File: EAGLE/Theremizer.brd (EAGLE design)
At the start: 160 x 100 mm, 121 parts, among them IC2 NE5532D, IC3 TL072D, J1 3x2 M, J2 1x6 M, J3 AUDIO_JACK_TRS_0.25"_PTH_RA, J4 POWER_JACK, J5 AUDIO_JACK_TRS_0.25"_PTH_RA, Q1 PMV45EN2R, Q2 J310, Q3 J310, Q4 J310, Q6 2N5088, Q7 2N5088, SW1 !RESET, U1 NCP1117ST50T3G, U2 MCU-ATMEGA328P-AU(TQFP32), U4 LTC2645CMS-L8PBF, X1 16 MHz

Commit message: Inital board & bunch of schematic changes
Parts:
- moved H1 255.4 mm to (156.2, 24.1)
- moved H2 253.3 mm to (156.2, 74.9)
- moved C6 198.0 mm to (87.6, 57.1), turned to 180 degrees
- moved TP6 197.4 mm to (88.9, 72.4)
- moved C28 190.1 mm to (119.4, 92.7)
- moved C20 186.0 mm to (57.1, 5.08), turned to 270 degrees
- moved R42 185.6 mm to (115.6, 83.8)
- moved TP5 185.1 mm to (81.3, 72.4)
- moved C15 184.7 mm to (124.5, 96.5)
- moved TP4 183.9 mm to (85.1, 72.4)
- moved C5 175.5 mm to (71.1, 63.5)
- moved J2 175.3 mm to (86.4, 80.0), turned to 180 degrees
- moved R38 173.0 mm to (124.5, 92.7)
- moved C4 169.6 mm to (71.1, 67.3)
- moved TP3 166.8 mm to (72.4, 72.4)
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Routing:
- net GND: track 0.00 -> 818.7 mm, vias 0 -> 2
- net +15V: track 0.00 -> 365.8 mm, vias 0 -> 1
- net -15V: track 0.00 -> 279.4 mm, vias 0 -> 2
- net +5V: track 0.00 -> 212.9 mm, vias 0 -> 3
- net N$52: track 0.00 -> 125.0 mm, vias 0 -> 1
- net N$19: track 0.00 -> 106.4 mm, vias 0 -> 2
- net RES_CV: track 0.00 -> 100.7 mm, vias 0 -> 6
- net N$50: track 0.00 -> 90.5 mm, vias 0 -> 2
- net N$24: track 0.00 -> 89.2 mm
- net N$6: track 0.00 -> 85.3 mm
- net THEREMIN_OUT: track 0.00 -> 79.6 mm, vias 0 -> 2
- net N$28: track 0.00 -> 78.5 mm
- net N$11: track 0.00 -> 75.8 mm, vias 0 -> 1
- net FREQ_CV: track 0.00 -> 74.8 mm, vias 0 -> 2
- net N$12: track 0.00 -> 71.6 mm, vias 0 -> 2
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- added copper zone on layer 1, net GND
- added copper zone on layer 16, net GND

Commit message: Package size change
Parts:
- C10, C12, C9: device rcl:C0402 -> rcl:C0805
- C18: value 100nF -> 100n
- C25: value (none) -> 100n
- IC1: value (none) -> AS3320
- R10, R12, R13, R14, R15, R16, R17, R18, R19, R21, R22, R23, R46, R48, R7, R9: device rcl:R0402 -> rcl:R0805
- U3: value (none) -> DCWN03B-15
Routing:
- net -15V: track 279.4 -> 280.9 mm
- net FILTER_OUTPUT: track 51.5 -> 52.8 mm
- net N$13: track 17.0 -> 18.3 mm
- net N$10: track 62.5 -> 63.4 mm
- net N$14: track 30.2 -> 31.1 mm
- net N$7: track 45.6 -> 46.5 mm

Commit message: Almost complete BOM
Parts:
- C11, C13, C14, C15, C16, C17, C18, C19, C20, C21, C23, C24, C25, C26, C27, C28, C29, C30, C31, C32: device rcl:C0402 -> rcl:C0805
- R24, R25, R28, R29, R30, R31, R32, R33, R38, R39, R40, R41, R42: device rcl:R0402 -> rcl:R0805
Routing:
- net GND: track 819.0 -> 821.6 mm
- net +15V: track 365.8 -> 368.0 mm
- net N$31: track 12.2 -> 13.5 mm
- net N$44: track 44.7 -> 45.6 mm
- net N$49: track 24.4 -> 25.3 mm
- net N$28: track 78.5 -> 79.4 mm
- net N$29: track 39.6 -> 40.5 mm
- net N$42: track 2.66 -> 1.91 mm
- net N$45: track 21.5 -> 22.1 mm
- net N$43: track 5.86 -> 6.38 mm
- net N$25: track 3.32 -> 3.84 mm

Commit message: Test point for filter out
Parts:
- added FILTER_OUT: TPB2,54, testpad:B2,54
- C1, C2, C3, C35, C4, C5, C6, C7, C8: device rcl:C0805K -> rcl:C0805
- C10, C12, C13, C21, C9: value 300pF -> 300p
- C20: value 100nF -> 100n
- C33, C34: value (none) -> 8-100p
- L2: value 10mH -> 10m
- R11: device rcl:R0402 -> rcl:R0805
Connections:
- net FILTER_OUTPUT: now also FILTER_OUT.TP

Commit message: Added bypass, new mixer
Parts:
- removed MX1: ADE-1, minickts (1):CD636
- added $U1: SA602AD, SA602AN:SO8
- added C36, C37: 0.1u, rcl:C0805
- added C38, C39: 10u, rcl:C0805
- added C40, C41: 10n, rcl:C0805
- added D4: M7, diode:SMB
- added IC4: NE5532D, linear:SO08
- added LD1: (no value), led:DUOLED-C-5MM
- added R20, R49: 0, rcl:R0805
- added R50: 10k, rcl:R0805
- added S2: SWITCH-3PDT-PTH-STOMP, SparkFun-Switches:STOMP_SWITCH_3PDT
- C18, C20, C25: value 100n -> 0.1u
- C21: value 300p -> 470n
- C23: value 2.2nF -> 2.2n
- C24: value 470pF -> 470p
- C26: value 10uF -> 10u
- C27: value 10n -> 200p
- C28: value 10n -> 4.7n
- C31: value 100u -> 1000u
- C34: value 8-100p -> 50-100p
- R25, R30: value 100 -> 100k
- R26: value 10k -> 1k; device pot:PT-10 -> rcl:R0805
- R34: value 10k -> 22k
- R35: device pot:PT-10 -> rcl:R0805
- R38, R39: value 470 -> 470k
- R41, R42: value 10k -> 100k
- R8: value DNP or 0 -> 0
- moved R26 329.9 mm to (-156.2, -61.0), turned to 0 degrees
- moved R35 315.2 mm to (-165.1, -92.7), turned to 0 degrees
- moved C27 278.4 mm to (-156.2, -54.6), turned to 0 degrees
- moved FILTER_OUT 179.5 mm to (6.35, 21.6)
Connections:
- removed net 9V: J4.PWR, U3.22, U3.23
- removed net AUDIO_INPUT: C11.1, J5.RING-NORM
- removed net N$32 (its old number): C15.1, C34.1
- new net +9V: $U1.8, S2.P$8
- new net AUDIO_IN: C11.1, S2.P$3
- new net N$38: R50.1, S2.P$4
- new net N$51: D1.A, D4.A, J4.PWR
- new net N$54: D4.C, U3.22, U3.23
- new net N$55: R20.1, U3.14
- new net N$56: R49.1, U3.11
- new net N$57: C26.1, L3.1, R29.2
- new net N$58: LD1.AX, S2.P$9
- new net OUTPUT: IC3.7, J3.RING-NORM, J3.TIP-NORM, R47.A, R47.S, S2.P$1, S2.P$6
- net +15V: now also C36.1, C37.1, C38.1, C39.1, IC4.8, R20.2; no longer D1.A, U3.14
- net -15V: now also R49.2; no longer IC2.4, U3.11
- net FILTER_OUTPUT: now also S2.P$5
- net GND: now also $U1.3, $U1.5, $U1.6, $U1.7, C15.1, C26.2, C36.2, C37.2, C38.2, C39.2, C40.1, IC2.4, IC4.4, LD1.C, Q2.G, Q3.G, R34.S, R50.2; no longer C27.2, J3.TIP-NORM, J5.SLEEVE-NORM, J5.TIP-NORM, MX1.1, MX1.4, MX1.5
- net N$22: now also C15.2
- net N$24: now also $U1.1; no longer MX1.6
- net N$26: now also C24.1, C27.1, L3.2, Q3.D; no longer C26.1, L3.1, R29.2
- net N$27: now also C27.2; no longer C24.1, L3.2, Q3.D
- net N$29: now also IC4.3; no longer IC2.5
- net N$33: now also C32.1, R35.2; no longer C15.2, Q2.G
- net N$35: now also C34.1
- net N$36: now also $U1.2; no longer MX1.3
- net N$37: now also J5.RING-NORM, J5.TIP-NORM, S2.P$2; no longer C26.2, Q3.G
- net N$39: now also R26.2; no longer R26.E
- net N$40: now also R26.1; no longer R26.A
- net N$47: now also J5.SLEEVE-NORM; no longer C32.1, R35.E
- net N$48: now also IC4.2, R35.1; no longer IC2.6, R35.A
- net N$49: now also IC4.1; no longer IC2.7
- net N$53: now also LD1.AR, S2.P$7; no longer IC3.7, J3.RING-NORM, R47.A, R47.S
- net THEREMIN_OUT: now also $U1.4, C40.2, C41.1, C41.2; no longer C27.1, MX1.2
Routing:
- net OUTPUT: track 0.00 -> 50.5 mm
- net N$53: track 50.5 -> 0.00 mm
- net N$57: track 0.00 -> 36.6 mm, vias 0 -> 2
- net GND: track 821.7 -> 788.5 mm
- net N$26: track 53.5 -> 20.8 mm, vias 2 -> 0
- net N$32 (its old number): track 24.4 -> 0.00 mm
- net N$24: track 88.9 -> 64.9 mm
- net N$40: track 30.3 -> 6.83 mm
- net N$27: track 21.1 -> 0.00 mm
- net N$36: track 20.8 -> 0.00 mm
- net 9V: track 20.5 -> 0.00 mm
- net AUDIO_INPUT: track 14.8 -> 0.00 mm
- net N$37: track 4.21 -> 17.3 mm
- net +15V: track 368.0 -> 356.9 mm
- net N$47: track 24.8 -> 14.2 mm
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
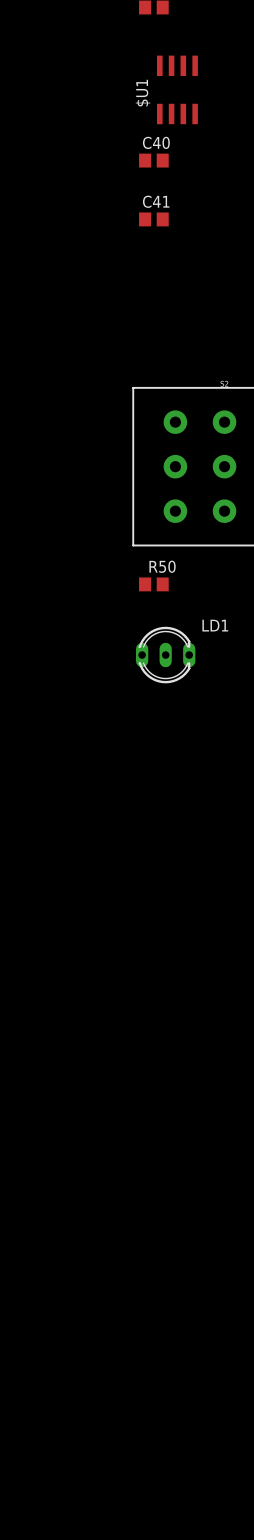
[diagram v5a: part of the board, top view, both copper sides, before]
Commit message: Changed cap values for mixer output, added decoupling caps, 9V regulator
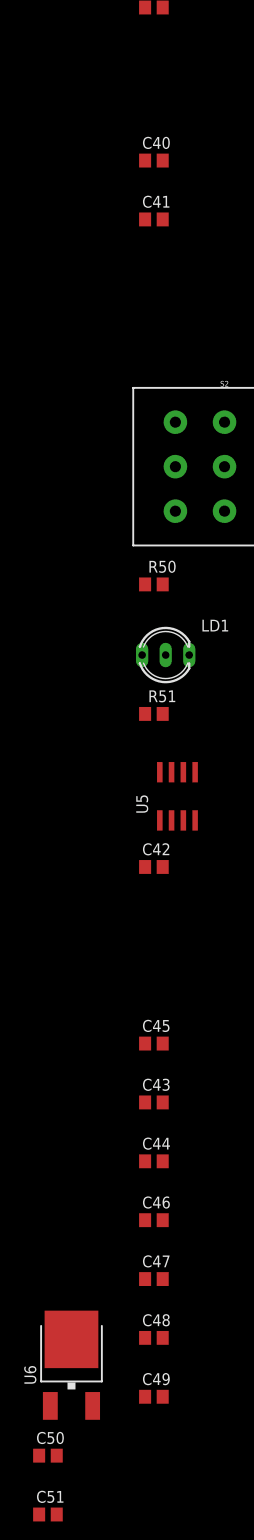
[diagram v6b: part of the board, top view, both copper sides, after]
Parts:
- removed $U1: SA602AD, SA602AN:SO8
- added C42, C43, C46, C48, C51: 0.1u, rcl:C0805
- added C44, C45, C47, C49: 10u, rcl:C0805
- added C50: 0.33u, rcl:C0805
- added R51: 1M, rcl:R0805
- added U5: (no value), SA602AN:SO8
- added U6: UA78M09, uA78Mx:DPACK
- C2: value 100n -> 0.1u
- C40: value 10n -> 1n
- C41: value 10n -> 47n
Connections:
- new net -15V1: C43.2, C44.2
- new net N$59: R51.1, U5.5
- net +15V: now also C48.2, C49.2
- net +9V: now also C51.1, U5.8, U6.3; no longer $U1.8
- net -15V: now also C42.2, C45.2, C46.2, C47.2
- net GND: now also C42.1, C43.1, C44.1, C45.1, C46.1, C47.1, C48.1, C49.1, C50.2, C51.2, R51.2, U5.3, U5.6, U5.7, U6.4; no longer $U1.3, $U1.5, $U1.6, $U1.7
- net N$24: now also U5.1; no longer $U1.1
- net N$36: now also U5.2; no longer $U1.2
- net N$51: now also C50.1, U6.1
- net THEREMIN_OUT: now also U5.4; no longer $U1.4

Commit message: Added decoupling caps and analog CV
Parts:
- added C52: 0.1u, rcl:C0805
- added C53: 10u, rcl:C0805
- added IC5: NE5532N, linear:DIL08
- added R52, R53, R54, R55: 100k, rcl:R0805
- added R56, R58: 51K, rcl:R0805
- added R57, R59: 100k, pot:ECP10P
- IC2, IC4: value NE5532D -> NE5532N; device linear:SO08 -> linear:DIL08
- R24, R29: device rcl:R0805 -> rcl:PRL1632
- R27: value 10k -> 470; device pot:PT-10 -> rcl:R0805
- moved R27 355.6 mm to (-176.5, -261.6)
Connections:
- removed net -15V1: C43.2, C44.2
- new net N$60: IC2.6, IC2.7
- new net N$61: IC2.5, R52.1, R53.2
- new net N$62: IC4.5, R54.1, R55.2
- new net N$63: IC4.6, IC4.7
- new net N$64: C23.1, C24.2, Q3.S, R27.1
- new net N$65: R58.1, R59.E
- net +15V: now also C43.2, C44.2; no longer C19.1, C20.1, C30.2, C36.1, C37.1, C38.1, C39.1, IC2.8, IC4.8, L4.1, Q6.1, Q7.1, R24.2, R25.2, R29.1, R41.1
- net +5V: now also R56.2, R58.2
- net +9V: now also C19.1, C20.1, C30.2, C36.1, C37.1, C38.1, C39.1, C52.1, C53.1, IC2.8, IC4.8, IC5.8, L4.1, Q6.1, Q7.1, R24.2, R25.2, R29.1, R41.1, R52.2, R54.2
- net FREQ_CV: now also R57.S
- net GND: now also C52.2, C53.2, IC5.4, R27.2, R53.1, R55.1, R57.A, R59.A; no longer R27.A, R27.S
- net N$32: now also R56.1, R57.E; no longer C23.1, C24.2, Q3.S, R27.E
- net RES_CV: now also R59.S
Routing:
- net +15V: track 356.9 -> 188.8 mm, vias 1 -> 0
- net +9V: track 0.00 -> 83.5 mm, vias 0 -> 1
- net N$32: track 15.1 -> 0.00 mm
- net N$64: track 0.00 -> 13.3 mm
- net GND: track 788.5 -> 777.7 mm
- net N$34: track 24.5 -> 16.4 mm
- net N$28: track 79.4 -> 74.6 mm
- net N$41: track 16.9 -> 18.7 mm
- net N$40: track 6.83 -> 7.87 mm

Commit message: Last BOM
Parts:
- removed C33: 8-100p, rcl:CTRIM808-BC
- removed C34: 50-100p, rcl:CTRIM808-BC
- removed C52: 0.1u, rcl:C0805
- removed C53: 10u, rcl:C0805
- removed IC5: NE5532N, linear:DIL08
- added JP1, JP2, JP3, JP4, JP5, JP6, JP7, JP8, JP9: (no value), jumper:JP1
- added PAD1, PAD2, PAD3: (no value), wirepad:2,15/1,0
- added R60: 470, rcl:R0805
- C11: value 100u -> 10u; device rcl:C0805 -> rcl:C050-025X075
- C14: value 1uF -> 1u
- C15, C26: device rcl:C0805 -> rcl:C050-025X075
- C19: value 10uF -> 10u
- C22, C35: value .1u -> 0.1u
- C28: value 4.7n -> 0.1u
- C29: value 10u -> 0.1u
- C31: value 1000u -> 470p
- C4, C6: value 100n -> 0.1u
- R1, R6: value 10K -> 10k
- R11, R15, R18, R22, R9: value 100K -> 100k
- R2, R3, R4, R5: value 1K -> 1k
- R40: value 10k -> 470
- R56, R58: value 51K -> 274k
- R57, R59: value 100k -> 10k
- U5: value (none) -> SA602AD
- moved R53 458.0 mm to (142.2, 54.6)
- moved R52 450.8 mm to (142.2, 50.8)
- moved R55 445.6 mm to (130.8, 35.6), turned to 180 degrees
- moved R54 439.2 mm to (127.0, 36.8), turned to 90 degrees
- moved R58 420.2 mm to (36.8, 26.7)
- moved R59 405.6 mm to (27.9, 25.4), turned to 180 degrees
- moved R56 403.9 mm to (36.8, 33.0)
- moved R57 403.4 mm to (27.9, 31.8)
- moved C51 391.1 mm to (33.0, 74.9), turned to 180 degrees
- moved C50 388.5 mm to (38.1, 74.9), turned to 180 degrees
- moved U6 381.3 mm to (48.3, 71.1), turned to 270 degrees
- moved C44 371.3 mm to (124.5, 15.2), turned to 90 degrees
- moved C43 370.5 mm to (124.5, 20.3), turned to 270 degrees
- moved C45 369.6 mm to (132.1, 15.2), turned to 90 degrees
- moved R27 362.6 mm to (54.6, 17.8)
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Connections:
- new net N$66: JP1.1, PAD2.1
- new net N$67: JP2.2, PAD3.1
- new net N$69: C27.1, JP3.2
- new net N$70: C25.2, JP4.1
- new net N$71: C29.1, JP5.2
- new net N$72: C28.1, JP6.2
- new net N$73: C32.2, JP7.2
- new net N$74: C18.2, JP8.2
- new net N$75: C41.1, JP9.1
- new net N$76: LD1.C, R60.1
- net +9V: no longer C52.1, C53.1, IC5.8
- net GND: now also C15.2, JP1.2, JP2.1, R60.2; no longer C15.1, C33.2, C34.2, C52.2, C53.2, IC5.4, LD1.C
- net N$22: now also C15.1; no longer C15.2
- net N$24: now also JP4.2; no longer C25.2
- net N$26: now also JP3.1; no longer C27.1, C33.1
- net N$35: now also JP6.1, PAD1.1; no longer C28.1, C34.1
- net N$36: now also JP8.1; no longer C18.2
- net N$41: now also JP5.1; no longer C29.1
- net N$45: now also JP7.1; no longer C32.2
- net THEREMIN_OUT: now also JP9.2; no longer C41.1
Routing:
- net +9V: track 83.5 -> 401.7 mm, vias 1 -> 7
- net GND: track 777.7 -> 906.1 mm, vias 2 -> 4
- net N$55: track 0.00 -> 123.1 mm
- net N$56: track 0.00 -> 112.1 mm, vias 0 -> 1
- net N$74: track 0.00 -> 96.9 mm, vias 0 -> 2
- net FILTER_OUTPUT: track 52.9 -> 142.6 mm, vias 2 -> 5
- net N$37: track 17.3 -> 92.9 mm
- net AUDIO_IN: track 0.00 -> 73.6 mm, vias 0 -> 1
- net RES_CV: track 101.0 -> 174.7 mm
- net N$51: track 0.00 -> 72.9 mm
- net N$34: track 16.4 -> 88.4 mm, vias 0 -> 2
- net N$59: track 0.00 -> 51.3 mm, vias 0 -> 2
- net OUTPUT: track 50.5 -> 101.2 mm
- net N$26: track 20.8 -> 67.7 mm
- net N$33: track 0.00 -> 41.9 mm
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- added copper zone on layer 1, net GND1
- removed copper zone on layer 1, net GND
